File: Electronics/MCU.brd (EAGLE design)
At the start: 50 x 50 mm, 14 parts, among them IC2 74AC157D, J77 uart, U1 ATMEGA2560-16AU-TQFP100, U2 AT25DF041A-SH-B

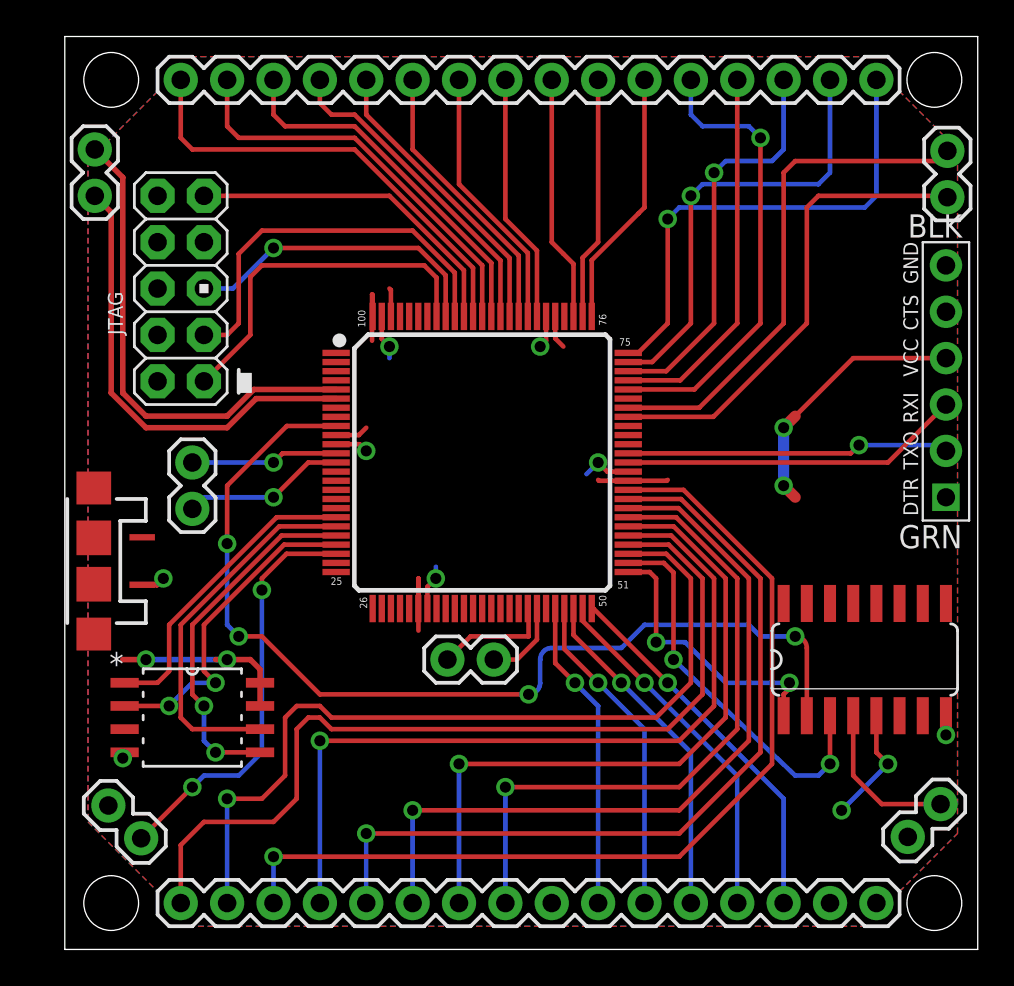
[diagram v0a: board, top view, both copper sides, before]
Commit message: Add uart0 breakout
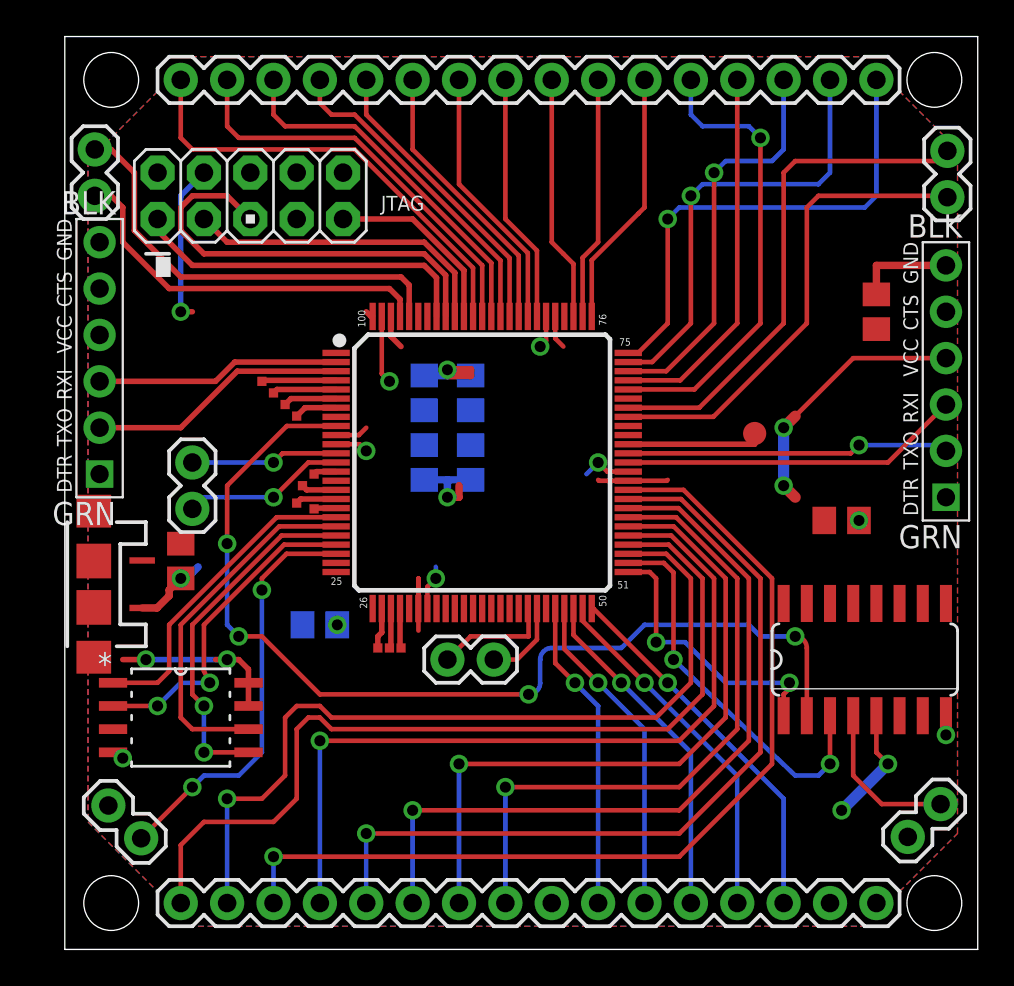
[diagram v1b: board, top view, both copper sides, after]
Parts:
- added C1, C2, C3, C4, C5, C6, C7, C8: (no value), rcl:C0805
- added JP9: FTDI_DEVICE, SparkFun-Connectors:FTDI_DEVICE_SIDE
- added TP1: TEST-POINT3X5, SparkFun:PAD.03X.05
- added TP10, TP11, TP13, TP2, TP3, TP4, TP5, TP6, TP7, TP8, TP9: TEST-POINT2, SparkFun:PAD.02X.02
- moved JP7 6.35 mm to (10.2, 41.3), turned to 90 degrees
- moved U$1 1.27 mm to (1.59, 20.0)
- moved U2 0.64 mm to (6.35, 12.7)
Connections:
- new net N$10: TP6.P$1, U1.17
- new net N$11: TP7.P$1, U1.16
- new net N$12: TP8.P$1, U1.4
- new net N$13: TP9.P$1, U1.14
- new net N$14: TP10.P$1, U1.6
- new net N$15: TP11.P$1, U1.7
- new net N$17: TP13.P$1, U1.5
- new net N$5: TP1.P$1, U1.65
- new net N$6: TP2.P$1, U1.28
- new net N$7: TP3.P$1, U1.29
- new net N$8: TP4.P$1, U1.27
- new net N$9: TP5.P$1, U1.18
- new net RX2: JP9.P$3, U1.2
- new net TX2: JP9.P$2, U1.3
- net GND: now also C1.2, C2.2, C3.2, C4.2, C5.2, C6.2, C7.2, C8.2
- net HALT: now also U1.97; no longer U1.6
- net INT: now also U1.96; no longer U1.5
- net VCC: now also C1.1, C2.1, C3.1, C4.1, C5.1, C6.1, C7.1, C8.1, U1.66, U1.67
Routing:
- net VCC: track 48.7 -> 64.7 mm, vias 6 -> 10
- net TX2: track 0.00 -> 14.2 mm
- net RX2: track 0.00 -> 13.4 mm
- net GND: track 16.0 -> 26.8 mm, vias 8 -> 9
- net TDI: track 18.5 -> 10.3 mm
- net N$5: track 0.00 -> 7.51 mm
- net TMS: track 17.0 -> 23.6 mm, vias 1 -> 0
- net TDO: track 21.7 -> 17.3 mm
- net N$12: track 0.00 -> 4.09 mm
- net HALT: track 24.9 -> 21.1 mm
- net N$17: track 0.00 -> 3.51 mm
- net N$14: track 0.00 -> 2.93 mm
- net INT: track 26.8 -> 23.9 mm
- net N$15: track 0.00 -> 2.35 mm
- net N$10: track 0.00 -> 2.25 mm
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
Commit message: Layout changes
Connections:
- net GND: now also IC2.15
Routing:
- net GND: track 26.8 -> 28.8 mm, vias 9 -> 10
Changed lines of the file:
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@@
 <wire x1="6.35" y1="20.32" x2="6.985" y2="20.6375" width="0.4064" layer="16"/>
 <wire x1="6.985" y1="20.6375" x2="7.3025" y2="20.955" width="0.4064" layer="16"/>
+<contactref element="IC2" pad="15"/>
+<wire x1="40.64" y1="18.9484" x2="40.64" y2="20.32" width="0.3048" layer="1"/>
+<via x="40.64" y="20.32" extent="1-16" drill="0.6" shape="octagon"/>
+<wire x1="40.64" y1="20.32" x2="40.64" y2="19.685" width="0.3048" layer="16"/>
 </signal>
 <signal name="WR">

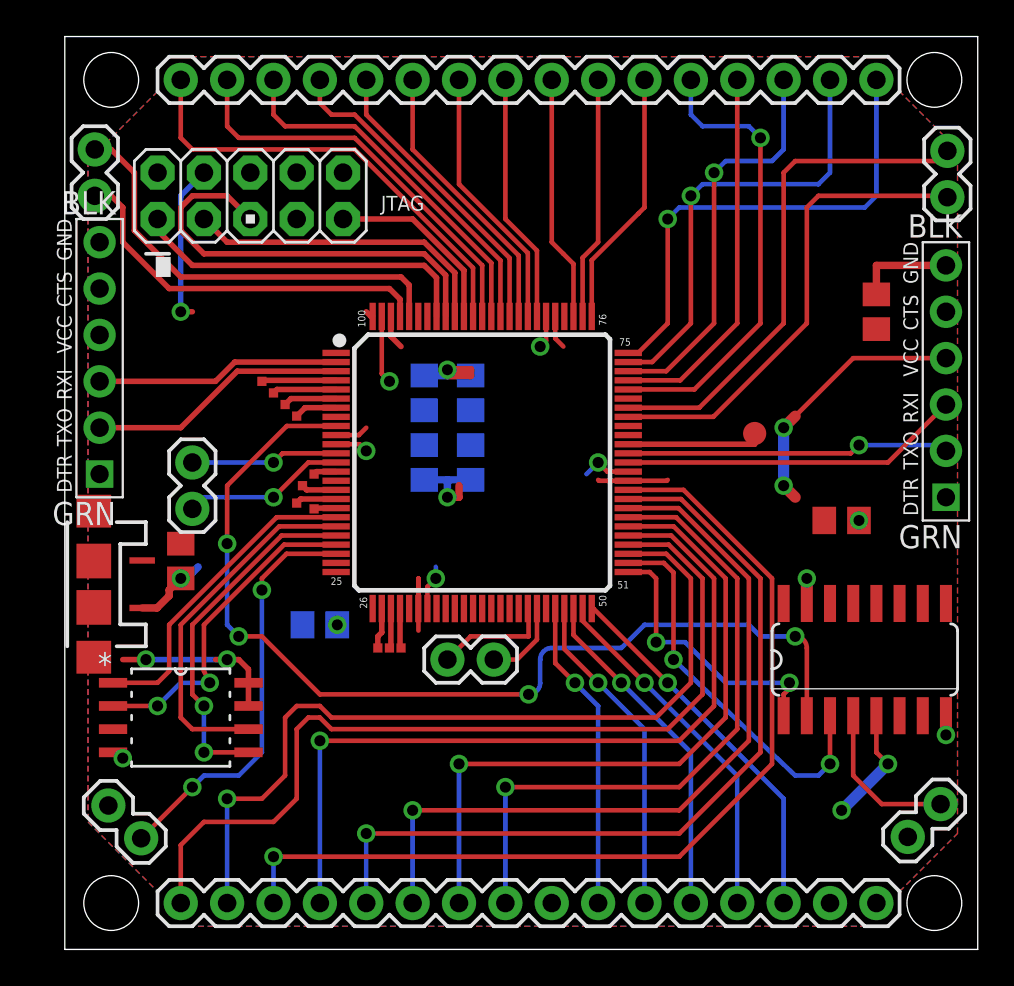
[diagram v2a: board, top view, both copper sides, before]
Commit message: Fix up caps on ram/mcu board
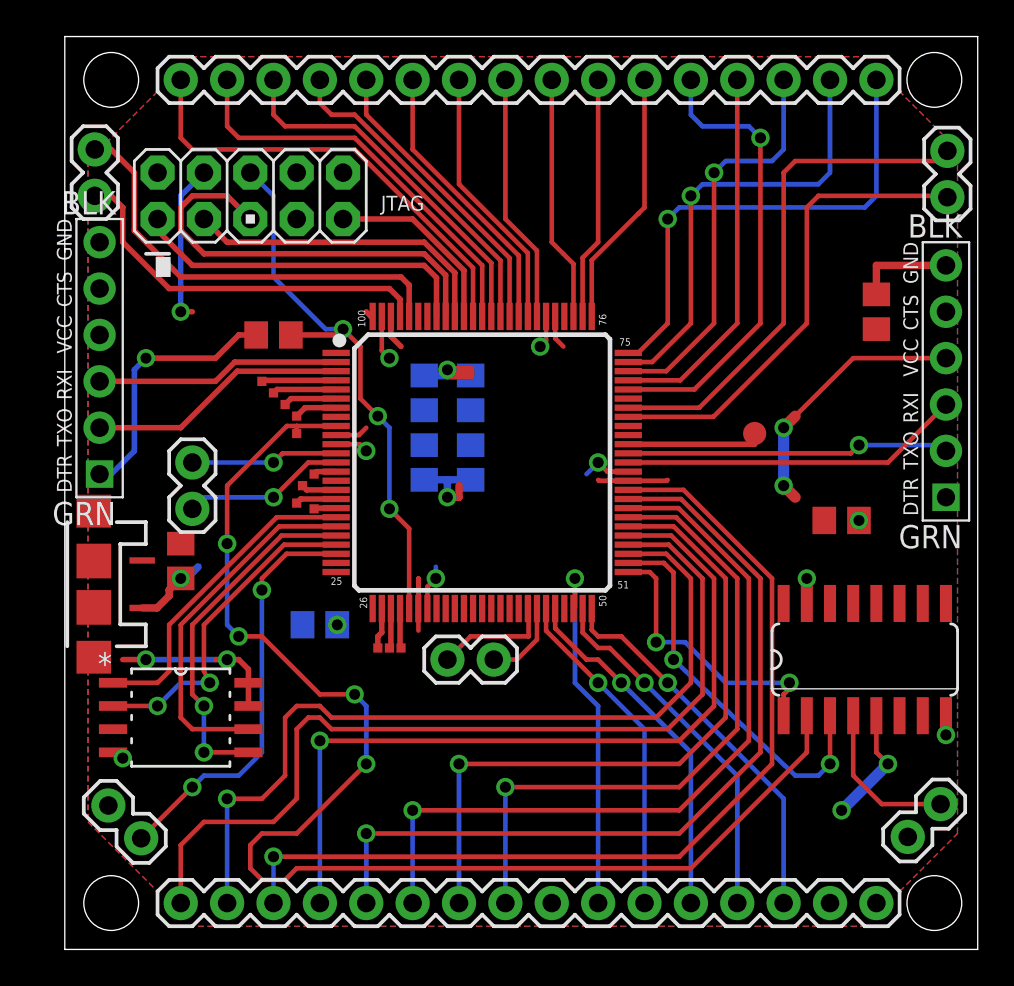
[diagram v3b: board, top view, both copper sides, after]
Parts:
- added C9: (no value), rcl:C0805
- added TP12: TEST-POINT2, SparkFun:PAD.02X.02
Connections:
- new net N$16: C9.2, JP9.P$1
- net /RESET: now also C9.1, U1.30
- net CLKO: now also TP12.P$1
- net GND: now also JP9.P$6
- net IORQ: now also U1.46; no longer U1.48
- net MREQ: now also U1.45; no longer U1.47
- net RESET: now also U1.48; no longer U1.46
- net VCC: now also JP9.P$4
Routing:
- net /RESET: track 0.00 -> 31.0 mm, vias 0 -> 3
- net CLKO: track 54.8 -> 73.1 mm
- net N$16: track 0.00 -> 14.3 mm, vias 0 -> 1
- net RESET: track 17.1 -> 20.0 mm
- net GND: track 28.8 -> 27.5 mm
- net IORQ: track 18.8 -> 19.6 mm
- net WR: track 20.5 -> 21.2 mm

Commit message: Update board outlines
Adding white line around boards for de-panelization
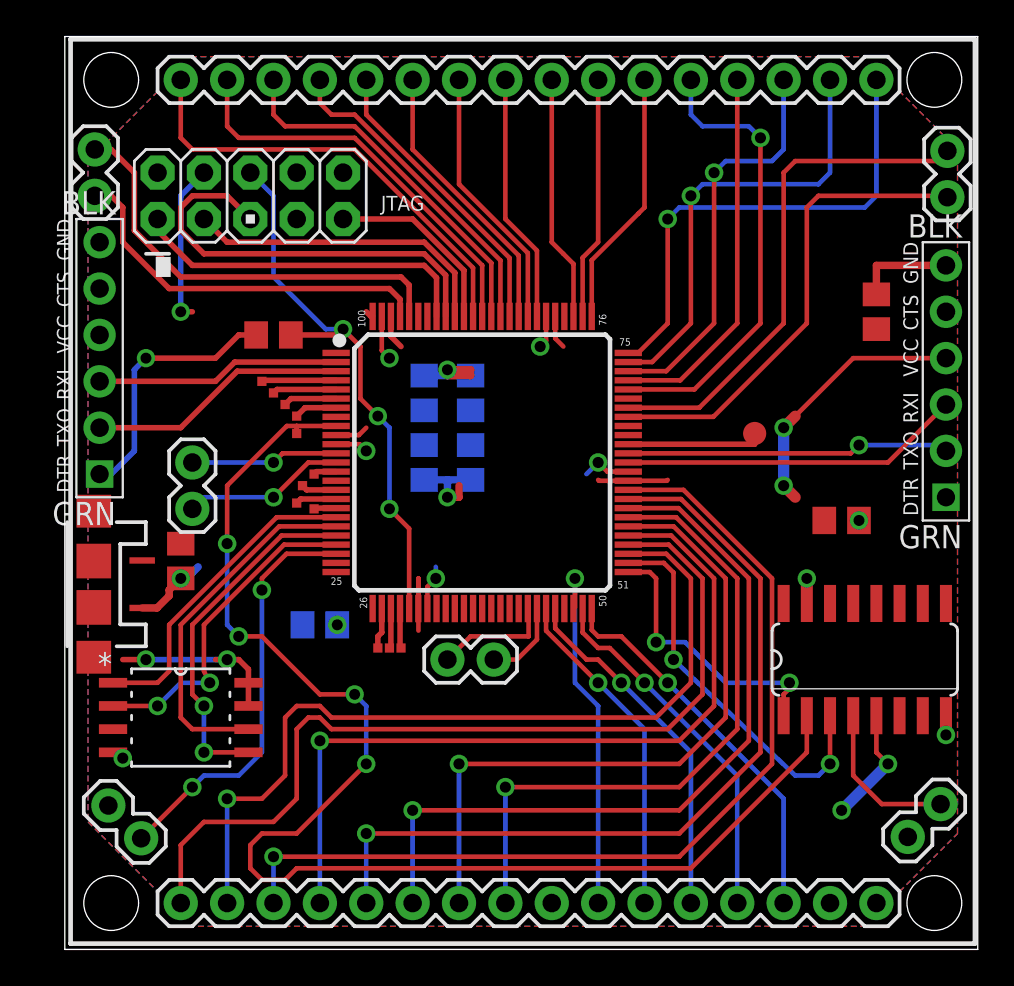
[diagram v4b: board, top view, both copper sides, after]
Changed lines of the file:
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@@
 <text x="19.685" y="41.275" size="0.8128" layer="21" rot="R180">JTAG</text>
 <text x="4.1275" y="36.83" size="6.4516" layer="21">.</text>
+<wire x1="49.8475" y1="49.8475" x2="0.3175" y2="49.8475" width="0.254" layer="21"/>
+<wire x1="0.3175" y1="49.8475" x2="0.3175" y2="0.3175" width="0.254" layer="21"/>
+<wire x1="0.3175" y1="0.3175" x2="49.8475" y2="0.3175" width="0.254" layer="21"/>
+<wire x1="49.8475" y1="0.3175" x2="49.8475" y2="49.8475" width="0.254" layer="21"/>
 </plain>
 <attributes>

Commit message: Route DIO Breakout + update Text
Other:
- board text added: "Ben V. Brown"
- board text added: "Project: Zeta"
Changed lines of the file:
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@@
 <wire x1="0.3175" y1="0.3175" x2="49.8475" y2="0.3175" width="0.254" layer="21"/>
 <wire x1="49.8475" y1="0.3175" x2="49.8475" y2="49.8475" width="0.254" layer="21"/>
+<text x="43.18" y="37.465" size="1.27" layer="22" font="vector" rot="MR0">Project: Zeta</text>
+<text x="41.91" y="31.75" size="0.8128" layer="21" font="vector" rot="R90">Ben V. Brown</text>
 </plain>
 <attributes>

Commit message: Gerbers!
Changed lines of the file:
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@@
 <wire x1="30.86" y1="31.67" x2="32.94" y2="31.67" width="0.254" layer="1"/>
 <wire x1="32.94" y1="31.67" x2="35.56" y2="34.29" width="0.254" layer="1"/>
-<wire x1="35.56" y1="34.29" x2="35.56" y2="42.545" width="0.254" layer="1"/>
-<via x="35.56" y="42.545" extent="1-16" drill="0.6096" shape="octagon"/>
-<wire x1="35.56" y1="42.545" x2="36.195" y2="43.18" width="0.254" layer="16"/>
-<wire x1="36.195" y1="43.18" x2="38.735" y2="43.18" width="0.254" layer="16"/>
+<wire x1="35.56" y1="34.29" x2="35.56" y2="43.18" width="0.254" layer="1"/>
+<via x="35.56" y="43.18" extent="1-16" drill="0.6096" shape="octagon"/>
+<wire x1="35.56" y1="43.18" x2="38.735" y2="43.18" width="0.254" layer="16"/>
 <wire x1="38.735" y1="43.18" x2="39.37" y2="43.815" width="0.254" layer="16"/>
 <wire x1="39.37" y1="43.815" x2="39.37" y2="47.625" width="0.254" layer="16"/>
@@
 <wire x1="30.86" y1="32.17" x2="32.17" y2="32.17" width="0.254" layer="1"/>
 <wire x1="32.17" y1="32.17" x2="34.29" y2="34.29" width="0.254" layer="1"/>
-<wire x1="34.29" y1="34.29" x2="34.29" y2="41.275" width="0.254" layer="1"/>
-<via x="34.29" y="41.275" extent="1-16" drill="0.6096" shape="octagon"/>
-<wire x1="34.29" y1="41.275" x2="34.925" y2="41.91" width="0.254" layer="16"/>
-<wire x1="34.925" y1="41.91" x2="41.275" y2="41.91" width="0.254" layer="16"/>
+<wire x1="34.29" y1="34.29" x2="34.29" y2="41.91" width="0.254" layer="1"/>
+<via x="34.29" y="41.91" extent="1-16" drill="0.6096" shape="octagon"/>
+<wire x1="34.29" y1="41.91" x2="41.275" y2="41.91" width="0.254" layer="16"/>
 <wire x1="41.275" y1="41.91" x2="41.91" y2="42.545" width="0.254" layer="16"/>
 <wire x1="41.91" y1="42.545" x2="41.91" y2="47.625" width="0.254" layer="16"/>

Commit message: Expanding bus driver
Added basic features to control the bus lines
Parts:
- renumbered UART1 to J11
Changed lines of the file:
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@@
 <element name="IC2" library="74xx-eu" package="SO16" value="74AC157D" x="43.815" y="15.875" smashed="yes"/>
 <element name="J77" library="SparkFun" package="1X02" value="uart" x="6.985" y="26.67" smashed="yes" rot="R270"/>
-<element name="UART1" library="SparkFun" package="1X02" value="i2c" x="23.495" y="15.875" smashed="yes" rot="R180"/>
+<element name="J11" library="SparkFun" package="1X02" value="i2c" x="23.495" y="15.875" smashed="yes" rot="R180"/>
 <element name="C1" library="rcl" package="C0805" value="" x="44.45" y="34.925" smashed="yes" rot="R90">
 <attribute name="VALUE" x="46.99" y="33.655" size="1.27" layer="27" rot="R90"/>
@@
 <signal name="N$3">
 <contactref element="U1" pad="44"/>
-<contactref element="UART1" pad="1"/>
+<contactref element="J11" pad="1"/>
 <wire x1="25.86" y1="18.67" x2="25.86" y2="16.97" width="0.254" layer="1"/>
 <wire x1="25.86" y1="16.97" x2="24.765" y2="15.875" width="0.254" layer="1"/>
@@
 <signal name="N$4">
 <contactref element="U1" pad="43"/>
-<contactref element="UART1" pad="2"/>
+<contactref element="J11" pad="2"/>
 <wire x1="25.36" y1="18.67" x2="25.4" y2="18.63" width="0.254" layer="1"/>
 <wire x1="25.4" y1="18.63" x2="25.4" y2="17.145" width="0.254" layer="1"/>
